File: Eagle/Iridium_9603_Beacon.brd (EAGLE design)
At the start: 57.6 x 66 mm, 100 parts, among them CON4 uFL, J1 SS4-10-3.50-X-D, Q1 DMG3415U-7, Q2 DMG3415U-7, Q3 DMG3415U-7, Q4 DMG3415U-7, Q5 2N2222, U1 MCP111T-240E/TT, U2 SPX3819-3.3, U3 LTC3225EDDB#TRMPBF, U4 MPL3115A2LGA8, U5 ATSAMD21G18_QFN, U6 MAX-M8, U7 LT1634-1,25BMCMS8, X1 32.768

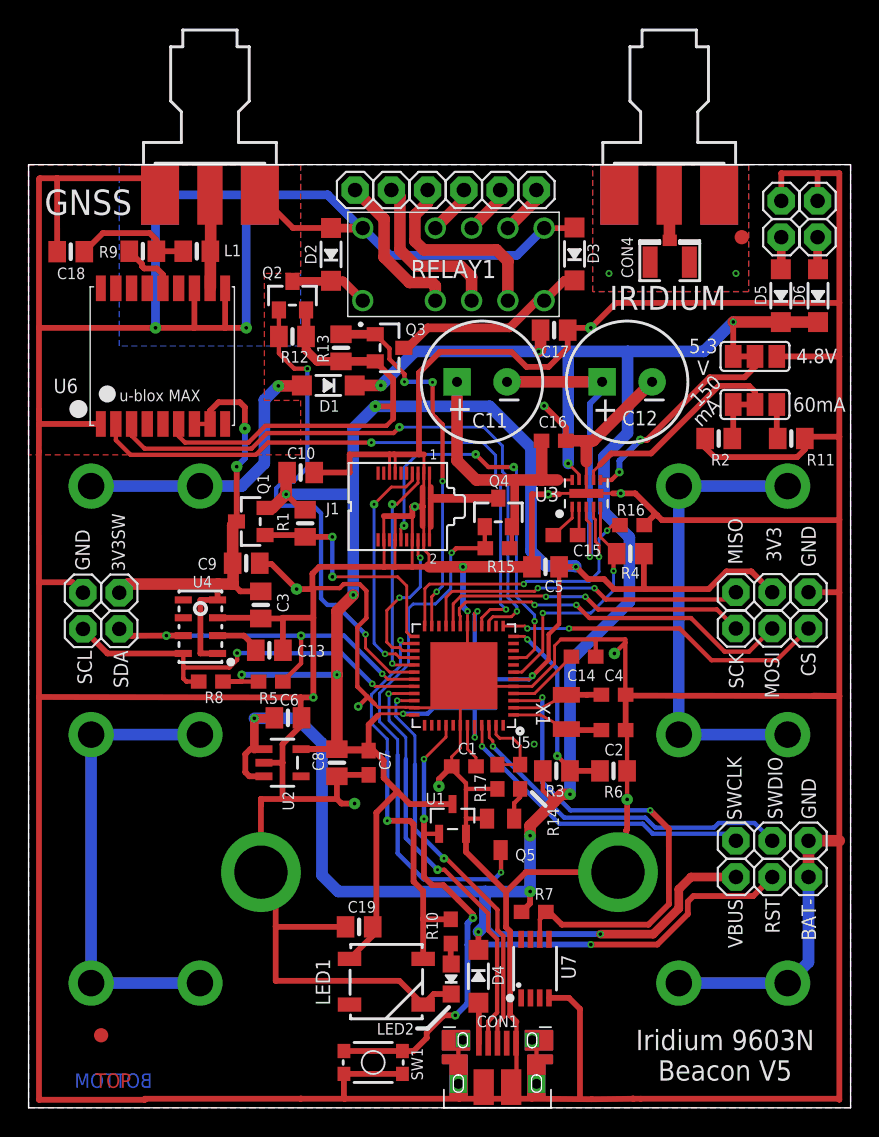
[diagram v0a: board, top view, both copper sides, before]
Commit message: Corrected the zero width polygons
Corrected the zero width polygons in the micro USB connector that were causing problems for OSH Park. Thanks go to Paul Loewen @ usask.ca
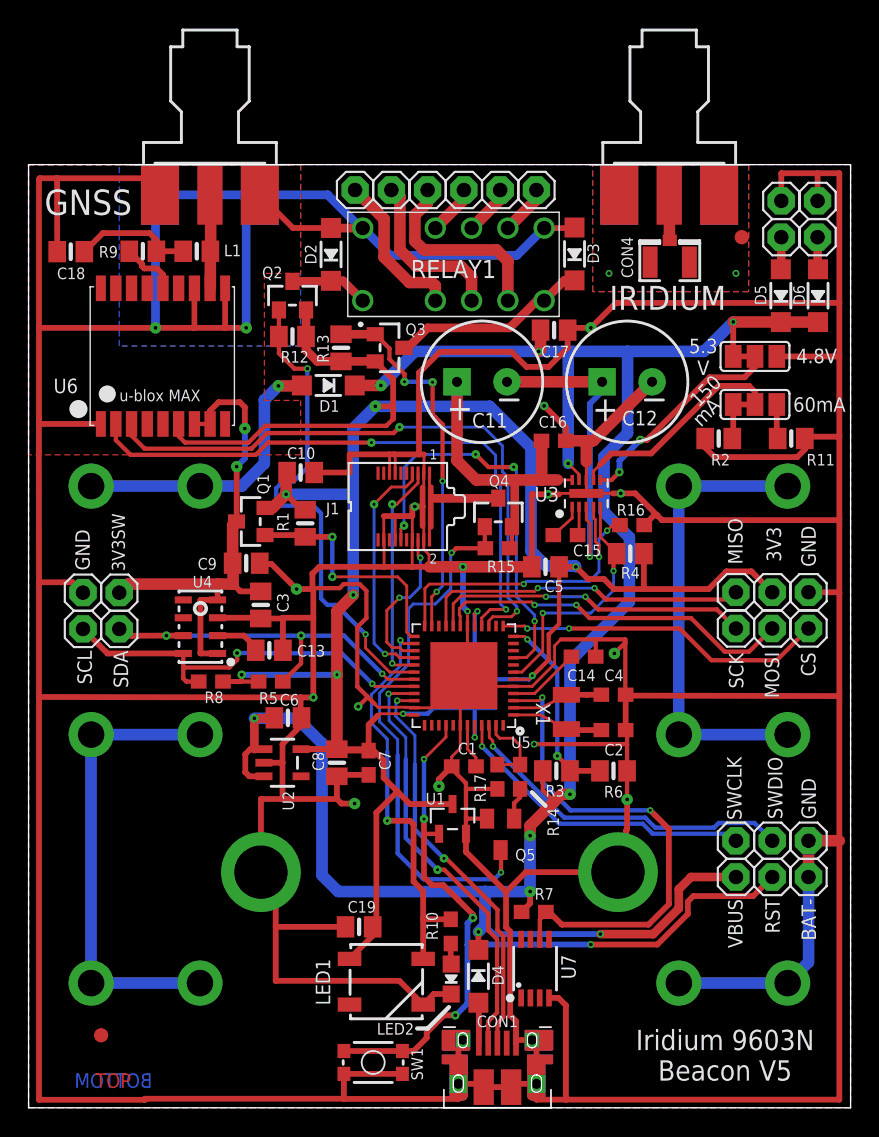
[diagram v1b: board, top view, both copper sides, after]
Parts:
- C2, C4: value 22pF -> 12pF
- CON1: device microbuilder:FCI_10103594 -> Iridium_9603_Beacon:MICROBUILDER_FCI_10103594_CORRECTED
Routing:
- net GND: track 692.6 -> 690.5 mm
- net +3V3: track 195.2 -> 193.9 mm
